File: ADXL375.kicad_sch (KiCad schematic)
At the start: 1 part, among them U6 ADXL372BCCZ-RL

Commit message: INA SENSOR
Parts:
- added C26, C27: 100nF, easyeda2kicad:C0402, symbol CANSAT_STM32_symbols:TCC0402X7R104J500AT
- added C28: 1uF, easyeda2kicad:CAP-SMD_L3.5-W2.8-R-RD, symbol CANSAT_STM32_symbols:TAJB105K035RNJ
- added L1: 0R 100Mhz, easyeda2kicad:L0402, symbol CANSAT_STM32_symbols:CBG100505U000T
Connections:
- net GND: now also C26.1, C27.1, C28.2
- net +3.3V: now reaches U6.1 (VDDI/O)
- net +3.3V: now also C26.2, L1.2
- net ACEL_INT1: now reaches U6.11 (INT1)
- net at U6.14 (VS): now also C27.2, C28.1, L1.1
- net ACEL_INT2: now reaches U6.9 (INT2)
- no-connect marks 3 -> 5
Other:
- moved on the sheet: U6

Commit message: BECERRA
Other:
- moved on the sheet: C26, C27, C28, L1, U6

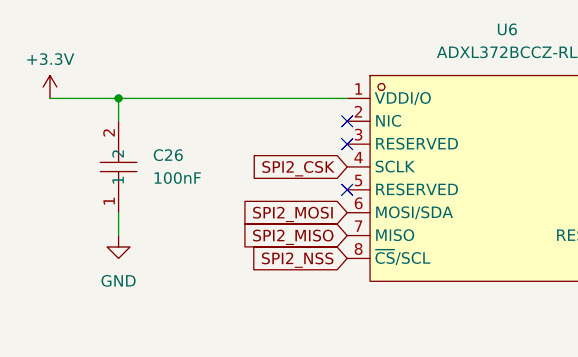
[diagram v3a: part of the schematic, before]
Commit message: Footprints V2
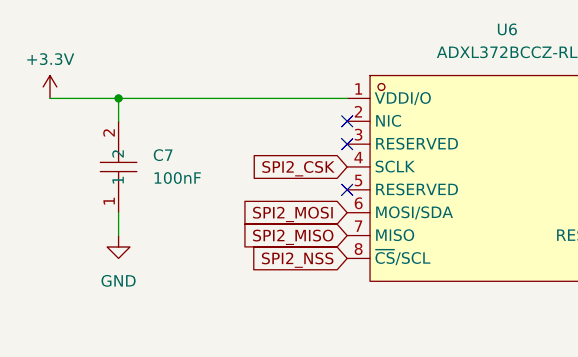
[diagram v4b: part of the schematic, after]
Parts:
- removed C26: 100nF, easyeda2kicad:C0402, symbol CANSAT_STM32_symbols:TCC0402X7R104J500AT
- added C7: 100nF, Capacitor_SMD:C_0402_1005Metric_Pad0.74x0.62mm_HandSolder, symbol CANSAT_STM32_symbols:TCC0402X7R104J500AT
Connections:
- net +3.3V: now also C7.2
- net GND: now also C7.1
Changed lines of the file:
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@@
 		(dnp no)
 		(fields_autoplaced yes)
-		(property "Reference" "C26"
+		(property "Reference" "C7"
 			(at 132.08 95.2499 90)
 			(show_name no)
@@
 			)
 		)
-		(property "Footprint" "easyeda2kicad:C0402"
+		(property "Footprint" "Capacitor_SMD:C_0402_1005Metric_Pad0.74x0.62mm_HandSolder"
 			(at 135.89 96.52 0)
 			(hide yes)
@@
 			(project "ARLISS_STM32_2026"
 				(path "/9719ea46-14c4-4409-9c57-49dd5454c03f/5dc414a7-f6ea-4307-9bff-662079fd3375"
-					(reference "C26")
+					(reference "C7")
 					(unit 1)
 				)

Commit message: Cantidad de errores en la PCB: 29
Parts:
- C27: footprint easyeda2kicad:C0402 -> ARLISS-footprints:C0402
- U6: footprint easyeda2kicad:LGA-16_L3.3-W3.0-P0.50-TL -> ARLISS-footprints:LGA-16_L3.3-W3.0-P0.50-TL
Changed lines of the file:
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@@
 			)
 		)
-		(property "Footprint" "easyeda2kicad:C0402"
+		(property "Footprint" "ARLISS-footprints:C0402"
 			(at 213.36 101.6 0)
 			(hide yes)
@@
 			)
 		)
-		(property "Footprint" "easyeda2kicad:LGA-16_L3.3-W3.0-P0.50-TL"
+		(property "Footprint" "ARLISS-footprints:LGA-16_L3.3-W3.0-P0.50-TL"
 			(at 171.45 114.3 0)
 			(hide yes)

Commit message: Cantidad de errores de la placa: 05
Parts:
- C28: footprint easyeda2kicad:CAP-SMD_L3.5-W2.8-R-RD -> ARLISS-footprints:CAP-SMD_L3.5-W2.8-R-RD
- L1: footprint easyeda2kicad:L0402 -> ARLISS-footprints:L0402
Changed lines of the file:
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@@
 			)
 		)
-		(property "Footprint" "easyeda2kicad:L0402"
+		(property "Footprint" "ARLISS-footprints:L0402"
 			(at 228.6 101.6 0)
 			(hide yes)
@@
 			)
 		)
-		(property "Footprint" "easyeda2kicad:CAP-SMD_L3.5-W2.8-R-RD"
+		(property "Footprint" "ARLISS-footprints:CAP-SMD_L3.5-W2.8-R-RD"
 			(at 226.06 101.6 0)
 			(hide yes)

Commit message: Primer Ruteo de PCB
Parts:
- C27: footprint ARLISS-footprints:C0402 -> Capacitor_SMD:C_0402_1005Metric_Pad0.74x0.62mm_HandSolder
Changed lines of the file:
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@@
 			)
 		)
-		(property "Footprint" "ARLISS-footprints:C0402"
+		(property "Footprint" "Capacitor_SMD:C_0402_1005Metric_Pad0.74x0.62mm_HandSolder"
 			(at 213.36 101.6 0)
 			(hide yes)
